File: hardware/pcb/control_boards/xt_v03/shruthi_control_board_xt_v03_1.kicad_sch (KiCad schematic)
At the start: 28 parts, among them IC1 24LC512, IC10 ATMEGA644p, J1 Conn_01x08, J3 M03PTH, J4 POWER, Q1 20MHz, U1 AVRISP, X1 MIDI, X2 MIDI

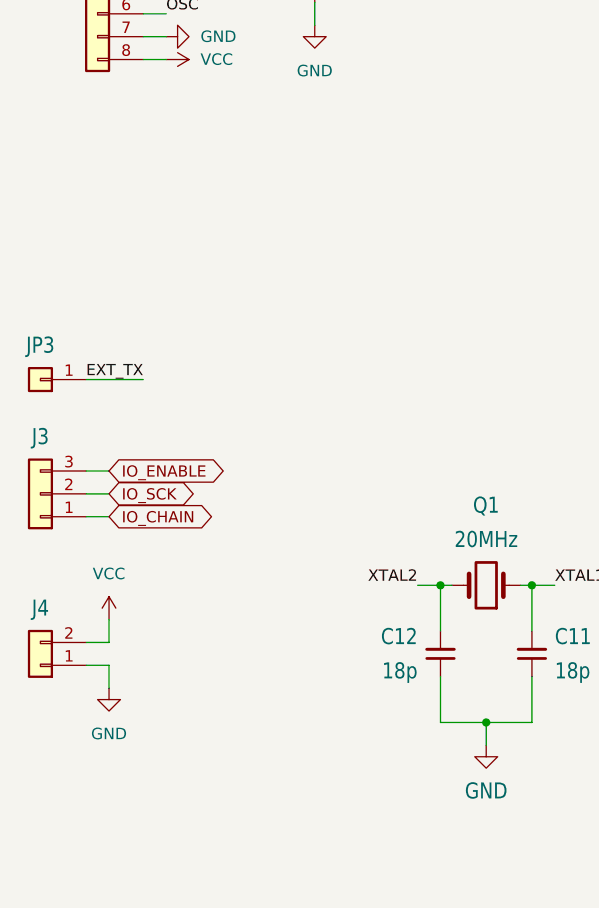
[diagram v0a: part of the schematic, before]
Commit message: update position of board to board connectors
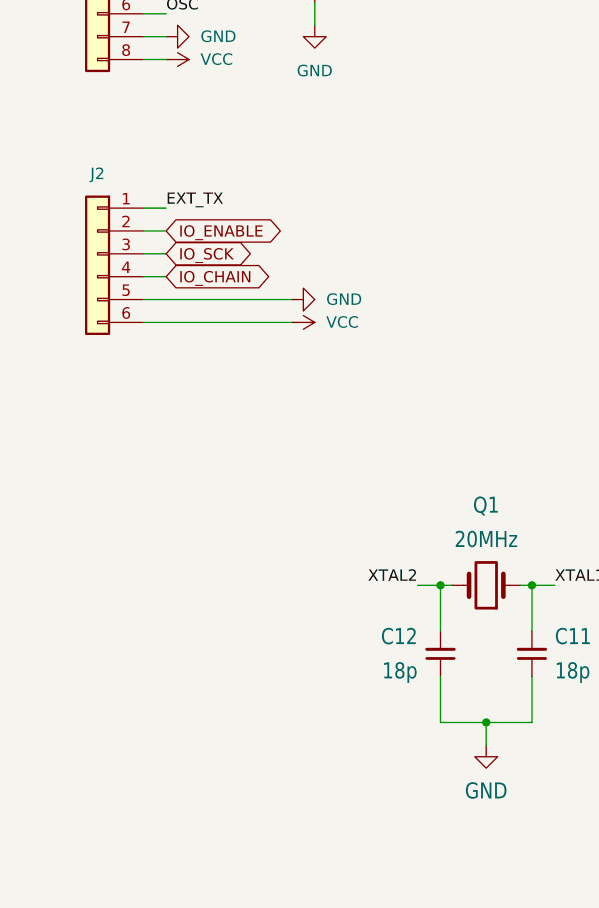
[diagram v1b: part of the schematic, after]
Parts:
- removed J3: M03PTH, shruthi_control_board_xt_v03:1X03, symbol Connector_Generic:Conn_01x03
- removed J4: POWER, shruthi_control_board_xt_v03:1X02, symbol Connector_Generic:Conn_01x02
- removed JP3: M01PTH, shruthi_control_board_xt_v03:1X01, symbol Connector_Generic:Conn_01x01
- added J2: Conn_01x06, Connector_PinHeader_2.54mm:PinHeader_1x06_P2.54mm_Vertical, symbol Connector_Generic:Conn_01x06
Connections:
- net EXT_TX: now also J2.1 (Pin_1)
- net GND: now also J2.5 (Pin_5)
- net IO_CHAIN: now also J2.4 (Pin_4)
- net IO_ENABLE: now also J2.2 (Pin_2)
- net IO_SCK: now also J2.3 (Pin_3)
- net VCC: now also J2.6 (Pin_6)

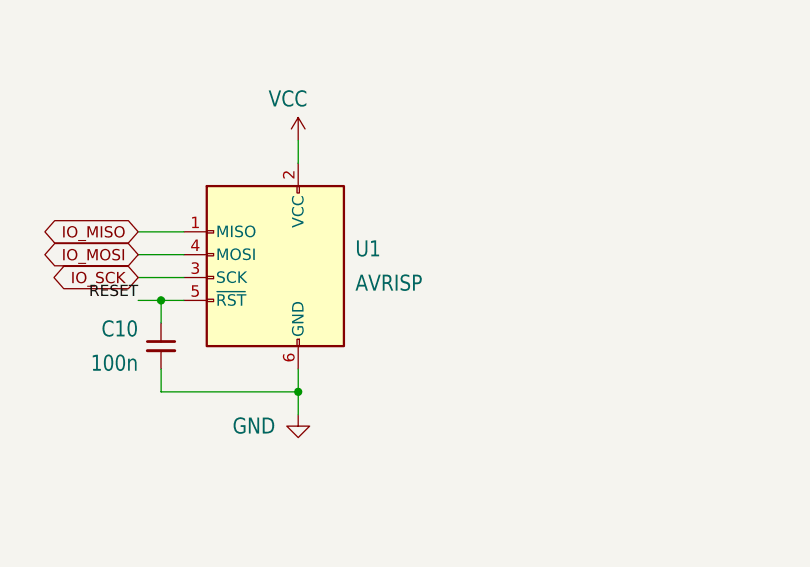
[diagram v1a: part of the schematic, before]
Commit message: update footprint and silkscreen for isp header
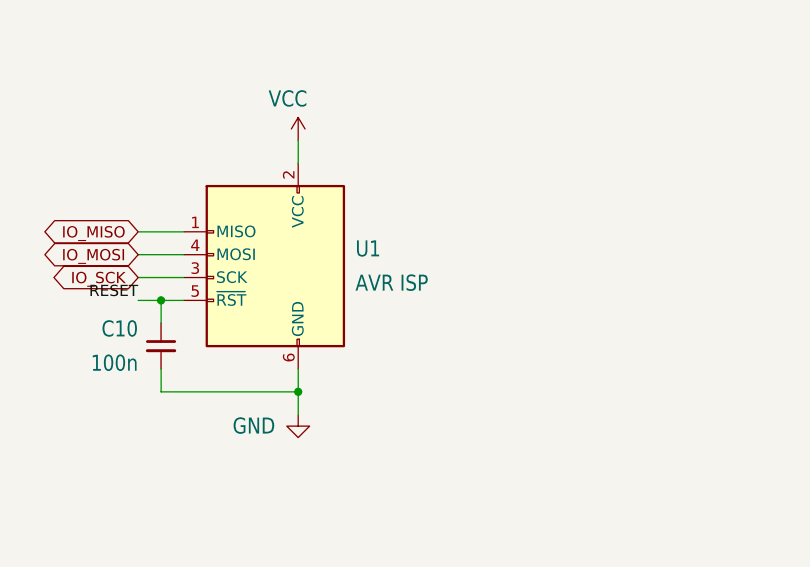
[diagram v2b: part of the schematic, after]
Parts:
- U1: value AVRISP -> AVR ISP; footprint shruthi_control_board_xt_v03:2X3 -> Connector_PinHeader_2.54mm:PinHeader_2x03_P2.54mm_Vertical
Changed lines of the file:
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@@
 			)
 		)
-		(property "Value" "AVRISP"
+		(property "Value" "AVR ISP"
 			(at 248.92 62.865 0)
 			(effects
@@
 			)
 		)
-		(property "Footprint" "shruthi_control_board_xt_v03:2X3"
+		(property "Footprint" "Connector_PinHeader_2.54mm:PinHeader_2x03_P2.54mm_Vertical"
 			(at 246.38 60.96 90)
 			(effects

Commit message: update footprints and silkscreen for optocoupler circuitry
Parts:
- D1: footprint shruthi_control_board_xt_v03:D-5 -> Diode_THT:D_DO-35_SOD27_P7.62mm_Horizontal
- R15, R16, R17, R18: footprint shruthi_control_board_xt_v03:0204_7 -> Resistor_THT:R_Axial_DIN0204_L3.6mm_D1.6mm_P7.62mm_Horizontal
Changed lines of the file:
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@@
 			)
 		)
-		(property "Footprint" "shruthi_control_board_xt_v03:0204_7"
+		(property "Footprint" "Resistor_THT:R_Axial_DIN0204_L3.6mm_D1.6mm_P7.62mm_Horizontal"
 			(at 335.28 82.55 0)
 			(effects
@@
 			)
 		)
-		(property "Footprint" "shruthi_control_board_xt_v03:0204_7"
+		(property "Footprint" "Resistor_THT:R_Axial_DIN0204_L3.6mm_D1.6mm_P7.62mm_Horizontal"
 			(at 373.38 81.28 0)
 			(effects
@@
 			)
 		)
-		(property "Footprint" "shruthi_control_board_xt_v03:0204_7"
+		(property "Footprint" "Resistor_THT:R_Axial_DIN0204_L3.6mm_D1.6mm_P7.62mm_Horizontal"
 			(at 336.55 121.92 0)
 			(effects
@@
 			)
 		)
-		(property "Footprint" "shruthi_control_board_xt_v03:0204_7"
+		(property "Footprint" "Resistor_THT:R_Axial_DIN0204_L3.6mm_D1.6mm_P7.62mm_Horizontal"
 			(at 361.95 121.92 0)
 			(effects
@@
 			)
 		)
-		(property "Footprint" "shruthi_control_board_xt_v03:D-5"
+		(property "Footprint" "Diode_THT:D_DO-35_SOD27_P7.62mm_Horizontal"
 			(at 340.36 87.63 90)
 			(effects

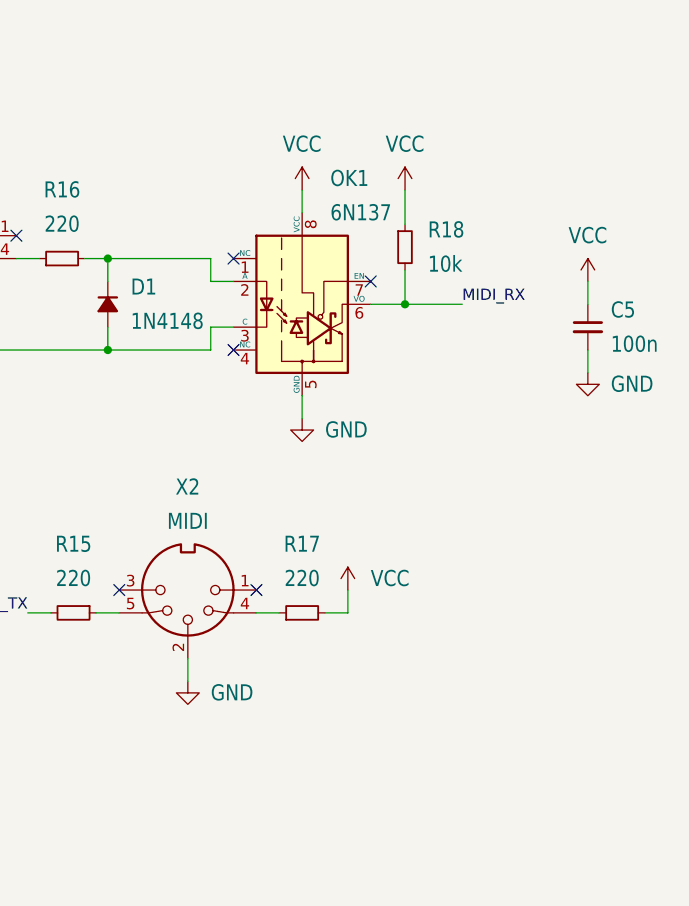
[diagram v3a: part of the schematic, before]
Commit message: update footprints and silkscreen for 24LC512 circuitry
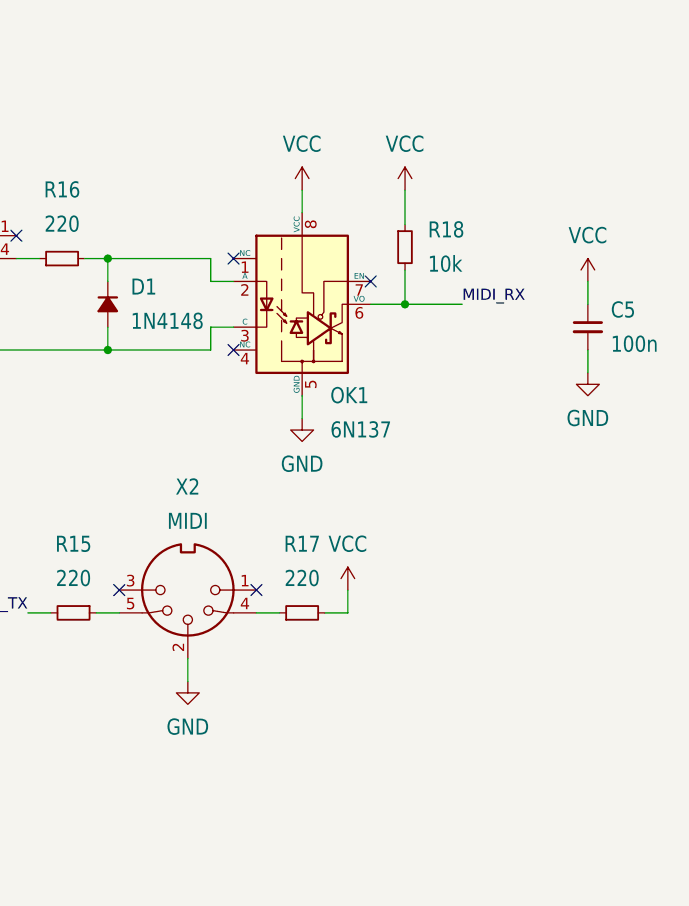
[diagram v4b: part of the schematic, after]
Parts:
- IC1: footprint shruthi_control_board_xt_v03:DIL08 -> Package_DIP:DIP-8_W7.62mm_Socket_LongPads
- R10, R9: footprint shruthi_control_board_xt_v03:0204_7 -> Resistor_THT:R_Axial_DIN0204_L3.6mm_D1.6mm_P7.62mm_Horizontal
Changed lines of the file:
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@@
 		)
 		(property "Value" "GND"
-			(at 351.79 130.81 0)
-			(effects
-				(font
-					(size 1.778 1.5113)
-				)
-				(justify left)
+			(at 349.25 134.62 0)
+			(effects
+				(font
+					(size 1.778 1.5113)
+				)
 			)
 		)
@@
 			)
 		)
-		(property "Footprint" "shruthi_control_board_xt_v03:0204_7"
+		(property "Footprint" "Resistor_THT:R_Axial_DIN0204_L3.6mm_D1.6mm_P7.62mm_Horizontal"
 			(at 227.33 137.16 0)
 			(effects
@@
 			)
 		)
-		(property "Footprint" "shruthi_control_board_xt_v03:DIL08"
+		(property "Footprint" "Package_DIP:DIP-8_W7.62mm_Socket_LongPads"
 			(at 240.03 147.32 0)
 			(effects
@@
 		)
 		(property "Value" "GND"
-			(at 364.49 101.6 0)
-			(effects
-				(font
-					(size 1.778 1.5113)
-				)
-				(justify left)
+			(at 361.95 105.41 0)
+			(effects
+				(font
+					(size 1.778 1.5113)
+				)
 			)
 		)
@@
 			)
 		)
-		(property "Footprint" "shruthi_control_board_xt_v03:0204_7"
+		(property "Footprint" "Resistor_THT:R_Axial_DIN0204_L3.6mm_D1.6mm_P7.62mm_Horizontal"
 			(at 224.79 137.16 0)
 			(effects
@@
 		)
 		(property "Value" "GND"
-			(at 396.24 96.52 0)
-			(effects
-				(font
-					(size 1.778 1.5113)
-				)
-				(justify left)
+			(at 393.7 100.33 0)
+			(effects
+				(font
+					(size 1.778 1.5113)
+				)
 			)
 		)
@@
 		)
 		(property "Value" "VCC"
-			(at 369.57 118.11 0)
-			(effects
-				(font
-					(size 1.778 1.5113)
-				)
-				(justify left)
+			(at 367.03 114.3 0)
+			(effects
+				(font
+					(size 1.778 1.5113)
+				)
 			)
 		)
@@
 		(fields_autoplaced yes)
 		(property "Reference" "OK1"
-			(at 365.0681 73.66 0)
+			(at 365.0681 97.79 0)
 			(effects
 				(font
@@
 		)
 		(property "Value" "6N137"
-			(at 365.0681 77.47 0)
-			(effects
-				(font
+			(at 365.0681 101.6 0)
+			(effects
+				(font

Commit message: update footprints and silkscreen for big cap
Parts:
- C4: footprint shruthi_control_board_xt_v03:E2,5-7 -> Capacitor_THT:CP_Radial_D6.3mm_P2.50mm
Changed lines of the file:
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@@
 			)
 		)
-		(property "Footprint" "shruthi_control_board_xt_v03:E2,5-7"
+		(property "Footprint" "Capacitor_THT:CP_Radial_D6.3mm_P2.50mm"
 			(at 55.88 31.75 0)
 			(effects
